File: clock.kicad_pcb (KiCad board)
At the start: 2 copper layers, 126 parts, among them J1 USB_C_Receptacle_USB2.0_16P, J2 Conn_01x02_Pin, J3 Conn_01x02_Pin, J4 Conn_01x02_Pin, Q1 2N7002K, Q2 NPN, U1 STM32F072CBT6, U2 USBLC6-2SC6, U4 MCP73871-2CC, U5 AP2112K-3.3

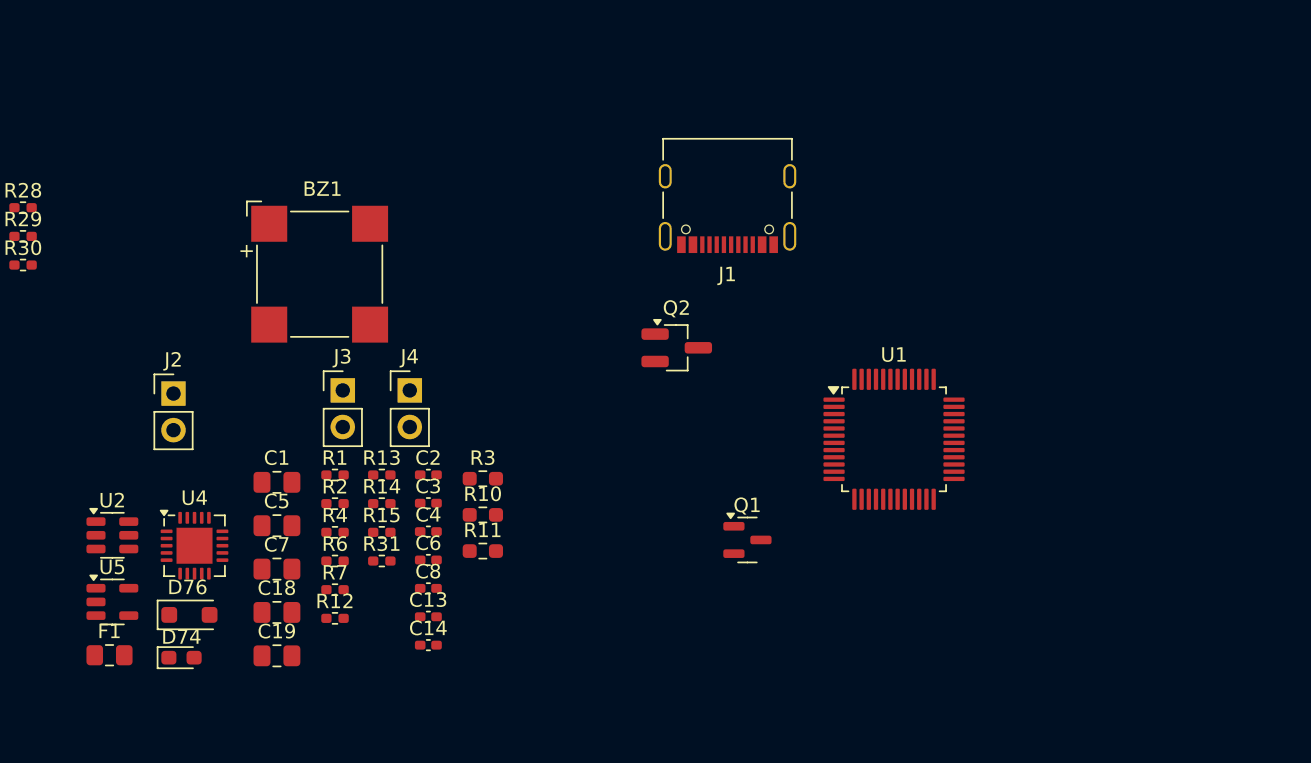
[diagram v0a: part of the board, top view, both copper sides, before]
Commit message: started layout, redid the crystal
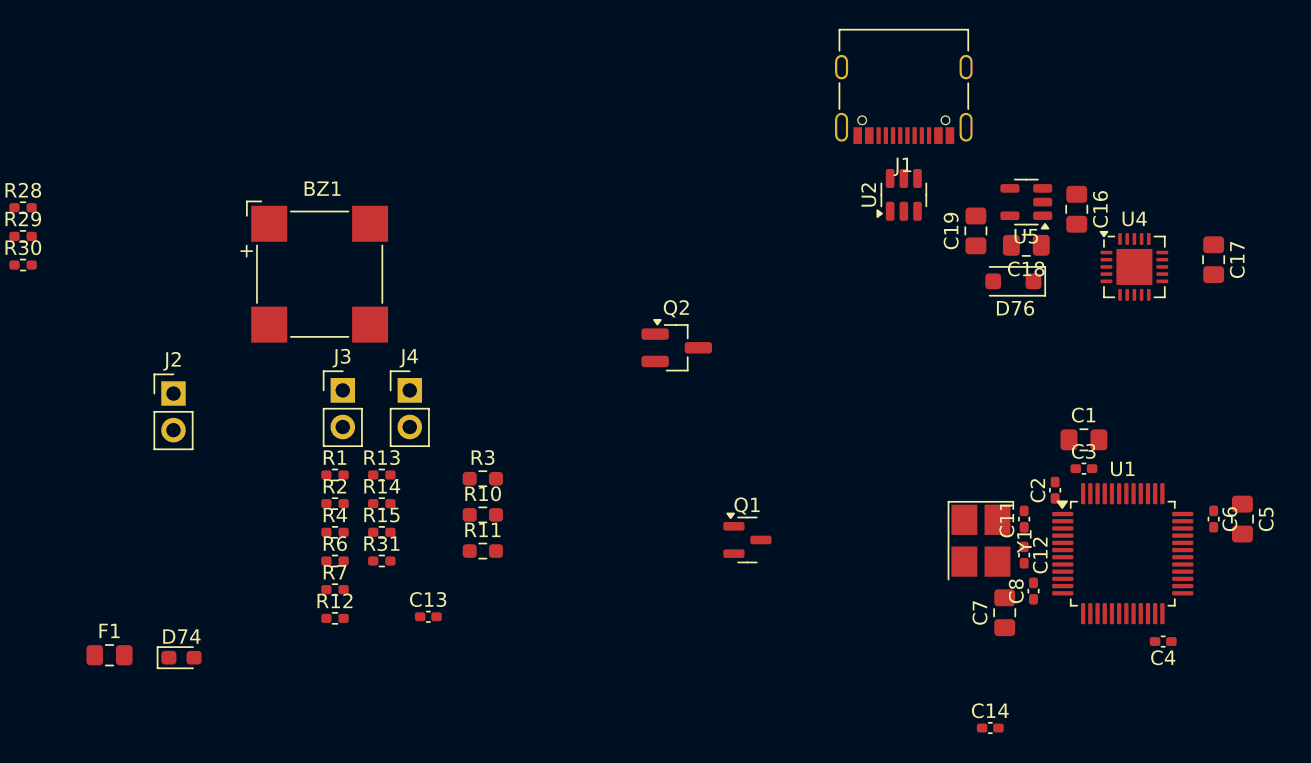
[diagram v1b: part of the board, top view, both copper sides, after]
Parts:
- added C11: 10pF, Capacitor_SMD:C_0402_1005Metric_Pad0.74x0.62mm_HandSolder, F.Cu at (209.8, 86.5)
- added C12: 10pF, Capacitor_SMD:C_0402_1005Metric_Pad0.74x0.62mm_HandSolder, F.Cu at (209.8, 89.0)
- added C16: 4.7uF, Capacitor_SMD:C_0805_2012Metric_Pad1.18x1.45mm_HandSolder, F.Cu at (213.5, 65.0)
- added C17: 4.7uF, Capacitor_SMD:C_0805_2012Metric_Pad1.18x1.45mm_HandSolder, F.Cu at (223.0, 68.5)
- added Y1: 8MHz, Crystal:Crystal_SMD_3225-4Pin_3.2x2.5mm_HandSoldering, F.Cu at (206.8, 88.0)
- moved U5 69.2 mm to (210.0, 64.5), turned to 180 degrees
- moved U4 68.0 mm to (217.5, 69.0)
- moved C5 67.0 mm to (225.0, 86.5), turned to -90 degrees
- moved D76 61.7 mm to (209.1, 70.0), turned to 180 degrees
- moved U2 59.8 mm to (201.5, 64.0), turned to 90 degrees
- moved C18 57.9 mm to (210.0, 67.5), turned to 180 degrees
- moved C19 56.8 mm to (206.5, 66.5), turned to 90 degrees
- moved C1 56.1 mm to (214.0, 81.0)
- moved C6 54.6 mm to (223.0, 86.5), turned to -90 degrees
- moved C4 51.6 mm to (219.5, 95.0), turned to 180 degrees
- moved C7 50.6 mm to (208.5, 93.0), turned to 90 degrees
- moved C3 45.6 mm to (214.0, 83.0)
- moved C2 43.5 mm to (212.0, 84.5), turned to 90 degrees
- moved C8 42.0 mm to (210.5, 91.5), turned to 90 degrees
- moved C14 39.4 mm to (207.5, 101.0)
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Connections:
- U1 pad 6: unconnected-(U1-PF1-Pad6) -> OSC_OUT

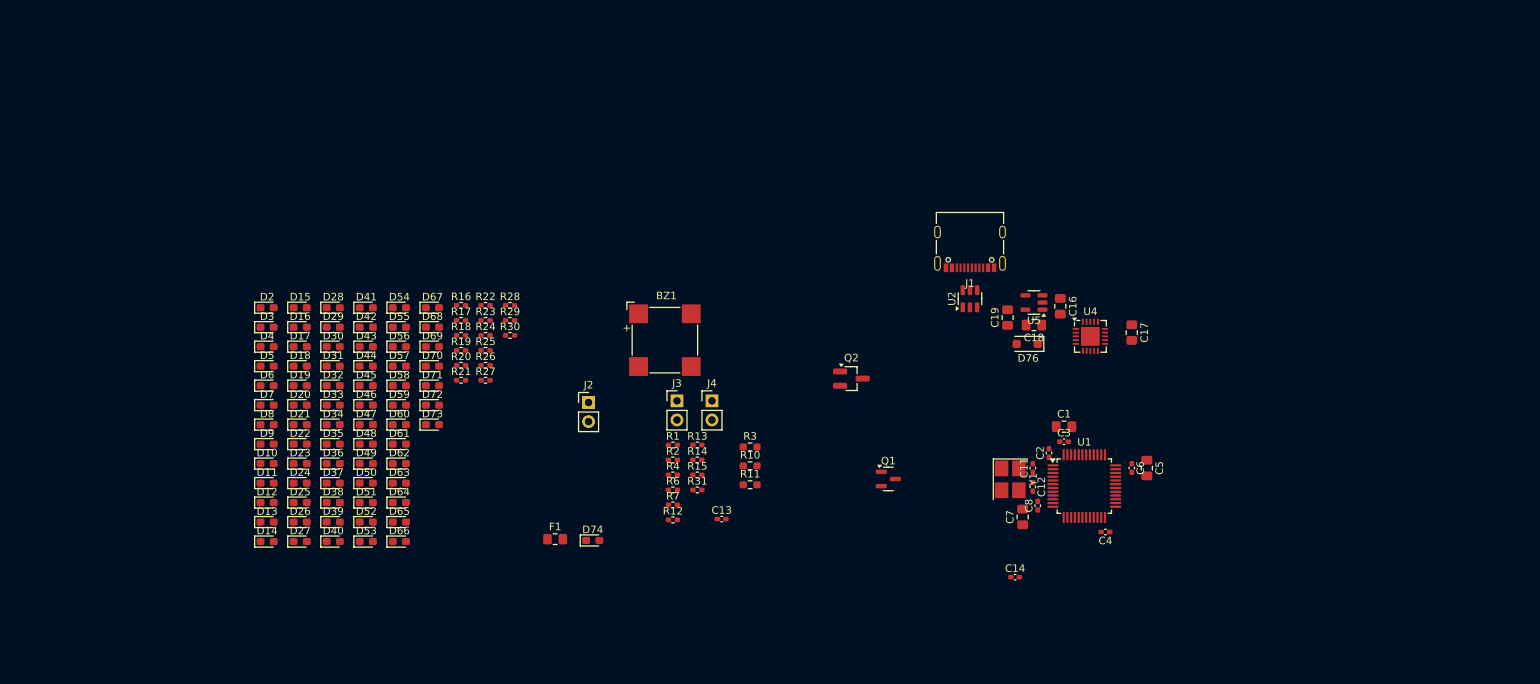
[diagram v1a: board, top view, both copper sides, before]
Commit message: layed out the LED display
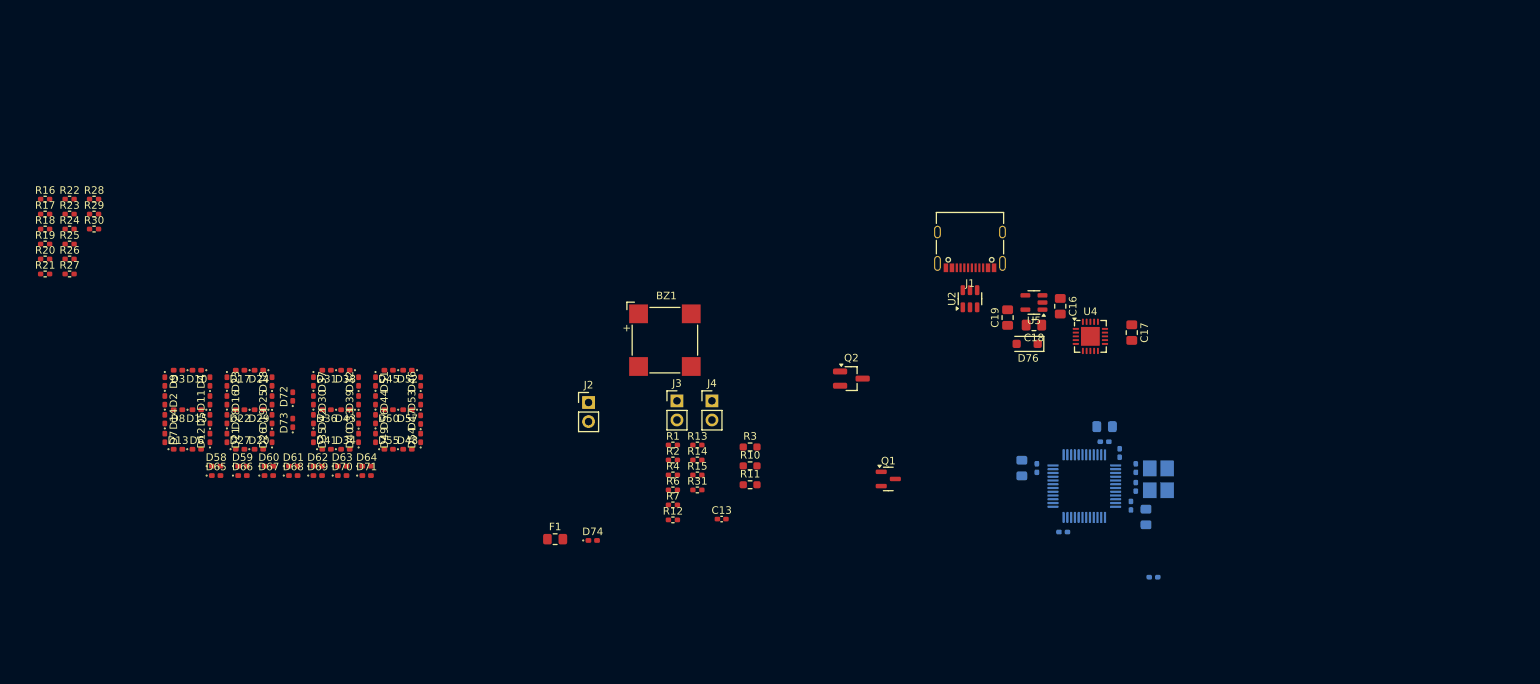
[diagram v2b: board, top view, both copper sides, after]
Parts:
- C1, C11, C12, C14, C2, C3, C4, C5, C6, C7, C8, U1, Y1: moved to B.Cu
- D10, D11, D12, D13, D14, D15, D16, D17, D18, D19, D2, D20, D21, D22, D23, D24, D25, D26, D27, D28, D29, D3, D30, D31, D32, D33, D34, D35, D36, D37, D38, D39, D4, D40, D41, D42, D43, D44, D45, D46, D47, D48, D49, D5, D50, D51, D52, D53, D54, D55, D56, D57, D58, D59, D6, D60, D61, D62, D63, D64, D65, D66, D67, D68, D69, D7, D70, D71, D72, D73, D74, D8, D9: footprint LED_SMD:LED_0603_1608Metric_Pad1.05x0.95mm_HandSolder -> LED_SMD:LED_0402_1005Metric_Pad0.77x0.64mm_HandSolder
- moved R16 57.1 mm to (78.6, 50.8)
- moved R17 57.1 mm to (78.6, 52.8)
- moved R18 57.1 mm to (78.6, 54.7)
- moved R19 57.1 mm to (78.6, 56.7)
- moved R20 57.1 mm to (78.6, 58.7)
- moved R21 57.1 mm to (78.6, 60.7)
- moved R22 57.1 mm to (81.8, 50.8)
- moved R23 57.1 mm to (81.8, 52.8)
- moved R24 57.1 mm to (81.8, 54.7)
- moved R25 57.1 mm to (81.8, 56.7)
- moved R26 57.1 mm to (81.8, 58.7)
- moved R27 57.1 mm to (81.8, 60.7)
- moved R28 57.1 mm to (85.1, 50.8)
- moved R29 57.1 mm to (85.1, 52.8)
- moved R30 57.1 mm to (85.1, 54.7)
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
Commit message: more layout
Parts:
- removed J2: Conn_01x02_Pin, Connector_PinHeader_2.54mm:PinHeader_1x02_P2.54mm_Vertical
- removed R3: 200k, Resistor_SMD:R_0603_1608Metric_Pad0.98x0.95mm_HandSolder
- moved J4 99.4 mm to (262.8, 105.0)
- moved R4 99.0 mm to (258.0, 111.5)
- moved J3 96.3 mm to (255.8, 102.0)
- moved BZ1 92.0 mm to (248.8, 42.0)
- moved R13 88.3 mm to (248.2, 53.2)
- moved C13 83.5 mm to (249.8, 112.8)
- moved Q2 67.1 mm to (248.2, 50.2)
- moved R6 65.0 mm to (225.2, 74.5)
- moved F1 57.3 mm to (195.7, 66.8)
- moved R2 54.3 mm to (209.3, 58.8)
- moved R1 54.0 mm to (209.3, 57.5)
- moved R10 53.9 mm to (219.8, 60.8)
- moved R11 53.9 mm to (219.8, 63.3)
- moved D74 52.3 mm to (202.0, 109.2)
- moved R14 42.2 mm to (202.1, 106.0)
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
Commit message: first attempt at layout
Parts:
- BZ1, C13, C16, C17, C18, C19, D74, D76, F1, J1, Q1, Q2, R1, R10, R11, R12, R13, R14, R15, R2, R31, R4, R6, R7, U2, U4, U5: moved to B.Cu
- moved BZ1 60.6 mm to (188.2, 42.0), turned to 180 degrees
- moved Q2 59.6 mm to (188.7, 50.2), turned to 180 degrees
- moved R13 59.6 mm to (188.7, 53.2), turned to 180 degrees
- moved C18 50.0 mm to (259.5, 74.6)
- moved R10 44.9 mm to (263.8, 69.8), turned to -90 degrees
- moved R28 44.4 mm to (97.2, 93.5)
- moved R11 43.8 mm to (263.5, 66.9), turned to 180 degrees
- moved R27 43.3 mm to (124.2, 69.2)
- moved R29 40.7 mm to (111.5, 83.8), turned to -90 degrees
- moved F1 36.2 mm to (231.8, 63.4), turned to -90 degrees
- moved R26 35.5 mm to (115.8, 69.2)
- moved U2 34.0 mm to (235.5, 63.8), turned to -90 degrees
- moved J1 33.9 mm to (235.4, 57.4), turned to 0 degrees
- moved R30 32.5 mm to (111.5, 73.8), turned to 90 degrees
- moved R25 25.1 mm to (103.5, 69.5)
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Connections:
- net Net-(F1-Pad1) renamed /VBUS
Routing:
- net GND: track 0.00 -> 41.2 mm
- net +5V: track 0.00 -> 32.5 mm, vias 0 -> 4
- net Net-(J1-CC2): track 0.00 -> 11.4 mm
- net VCC: track 0.00 -> 10.1 mm
- net /VBUS: track 0.00 -> 9.12 mm, vias 0 -> 2
- net Net-(J1-CC1): track 0.00 -> 6.97 mm
- net D_BUS-: track 0.00 -> 5.63 mm
- net D_BUS+: track 0.00 -> 4.96 mm
- net +3.3V: track 0.00 -> 2.57 mm

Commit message: changed R package sizes + moved stuff around
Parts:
- R10, R11: footprint Resistor_SMD:R_0603_1608Metric_Pad0.98x0.95mm_HandSolder -> Resistor_SMD:R_0402_1005Metric_Pad0.72x0.64mm_HandSolder
- moved R10 43.2 mm to (221.4, 61.6)
- moved R11 42.4 mm to (221.2, 64.0), turned to 90 degrees
- moved R6 13.2 mm to (223.2, 60.4)
- moved C16 1.00 mm to (215.0, 64.5)
- moved C19 1.00 mm to (217.9, 61.1)
- moved U5 1.00 mm to (218.0, 64.8)
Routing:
- net +5V: track 32.5 -> 27.7 mm, vias 4 -> 3
- net +3.3V: track 2.57 -> 7.06 mm
- net LBO: track 0.00 -> 1.92 mm
- net VCC: track 10.1 -> 11.2 mm
- net GND: track 41.2 -> 41.9 mm

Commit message: small routing changes, reverted action change
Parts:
- moved R12 47.1 mm to (229.6, 70.6), turned to -90 degrees
- moved Q1 41.9 mm to (226.6, 70.8)
- moved R7 40.4 mm to (225.0, 68.2), turned to 0 degrees
- moved R10 0.60 mm to (220.8, 61.6)
- moved R11 0.45 mm to (220.8, 64.2)
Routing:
- net +5V: track 27.7 -> 38.3 mm, vias 3 -> 4
- net Net-(Q1-D): track 0.00 -> 5.17 mm
- net Net-(U4-VPCC): track 0.00 -> 3.50 mm
- net GND: track 41.9 -> 44.7 mm
- net Net-(Q1-G): track 0.00 -> 2.12 mm

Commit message: routing attempt again
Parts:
- moved C17 69.9 mm to (260.5, 36.6), turned to 90 degrees
- moved R2 52.9 mm to (272.8, 29.2), turned to -90 degrees
- moved R1 50.0 mm to (272.8, 32.0), turned to 90 degrees
- moved D76 45.6 mm to (244.2, 33.8), turned to 90 degrees
- moved R6 45.2 mm to (256.2, 29.5), turned to 90 degrees
- moved U4 44.2 mm to (256.6, 33.6)
- moved R11 43.3 mm to (252.5, 34.8)
- moved R10 43.2 mm to (252.5, 32.2)
- moved C19 42.9 mm to (247.8, 30.4)
- moved U5 42.6 mm to (247.8, 34.4)
- moved U2 41.0 mm to (266.8, 37.2)
- moved J1 40.8 mm to (266.4, 30.8)
- moved F1 40.5 mm to (263.0, 37.5)
- moved C18 37.9 mm to (248.2, 38.4)
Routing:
- net GND: track 44.7 -> 19.7 mm
- net VCC: track 11.2 -> 17.8 mm
- net Net-(J5-Pin_1): track 0.00 -> 5.23 mm
- net Net-(Q1-D): track 5.17 -> 0.00 mm
- net Net-(J1-CC2): track 11.4 -> 6.38 mm
- net +5V: track 38.3 -> 34.1 mm
- net Net-(J1-CC1): track 6.97 -> 10.6 mm
- net Net-(Q1-G): track 2.12 -> 0.00 mm
- net LBO: track 1.92 -> 0.00 mm
- net /VBUS: track 9.12 -> 9.81 mm
- net Net-(U4-VPCC): track 3.50 -> 4.02 mm
- added copper zone on B.Cu, net GND
